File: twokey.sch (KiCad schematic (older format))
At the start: 10 parts, among them J1 12401610E4#2A, U1 ATSAMD21E18A-A, U2 MCP1700-3302E_SOT23

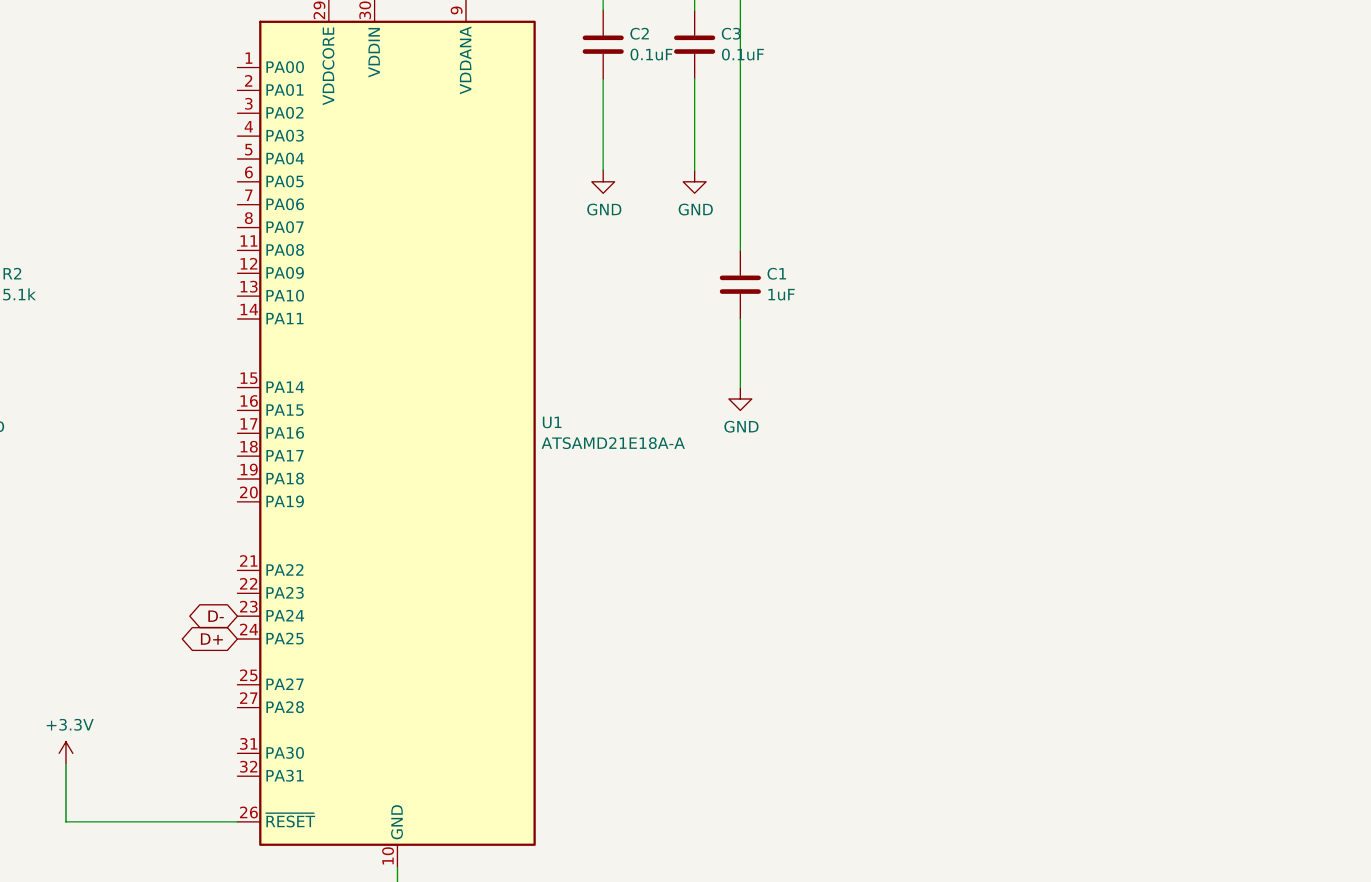
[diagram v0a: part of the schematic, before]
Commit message: added key switches
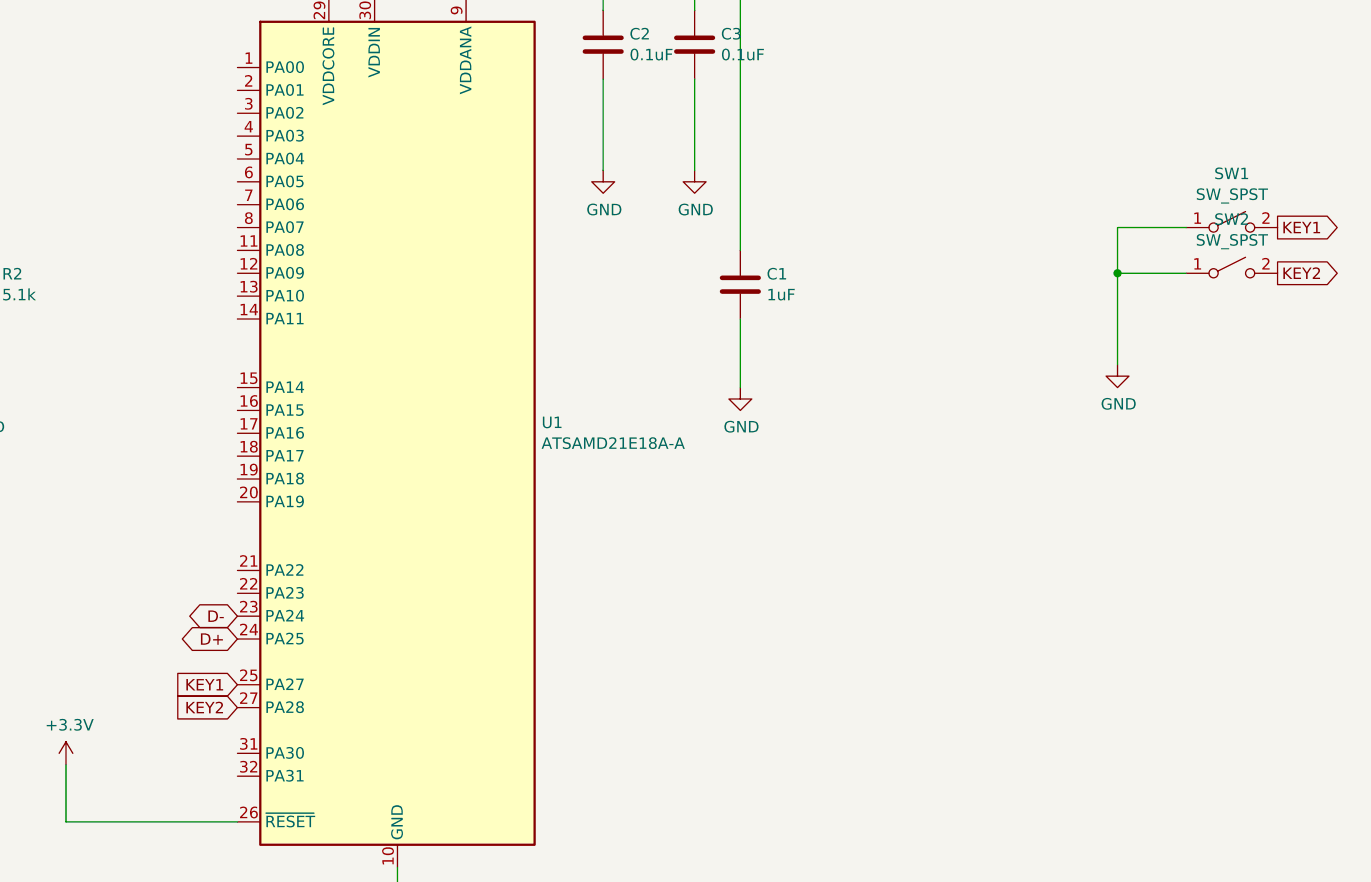
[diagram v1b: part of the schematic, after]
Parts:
- added SW1, SW2: SW_SPST, Button_Switch_Keyboard:SW_Cherry_MX_1.00u_PCB, symbol Switch:SW_SPST
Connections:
- net labels added: KEY1, KEY2
- wire segments 49 -> 53
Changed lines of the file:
@@
 Wire Wire Line
 	3450 3350 3450 3450
+$Comp
+L Switch:SW_SPST SW1
+U 1 1 60FA499B
+P 9150 2750
+F 0 "SW1" H 9150 2985 50  0000 C CNN
+F 1 "SW_SPST" H 9150 2894 50  0000 C CNN
+F 2 "Button_Switch_Keyboard:SW_Cherry_MX_1.00u_PCB" H 9150 2750 50  0001 C CNN
+F 3 "~" H 9150 2750 50  0001 C CNN
+	1    9150 2750
+	1    0    0    -1
+$EndComp
+Text GLabel 4800 4750 0    50   Input ~ 0
+KEY1
+Text GLabel 4800 4850 0    50   Input ~ 0
+KEY2
+Text GLabel 9350 2750 2    50   Output ~ 0
+KEY1
+$Comp
+L Switch:SW_SPST SW2
+U 1 1 60FA81CF
+P 9150 2950
+F 0 "SW2" H 9150 3185 50  0000 C CNN
+F 1 "SW_SPST" H 9150 3094 50  0000 C CNN
+F 2 "Button_Switch_Keyboard:SW_Cherry_MX_1.00u_PCB" H 9150 2950 50  0001 C CNN
+F 3 "~" H 9150 2950 50  0001 C CNN
+	1    9150 2950
+	1    0    0    -1
+$EndComp
+Text GLabel 9350 2950 2    50   Output ~ 0
+KEY2
+$Comp
+L power:GND #PWR016
+U 1 1 60FA8FBB
+P 8650 3350
+F 0 "#PWR016" H 8650 3100 50  0001 C CNN
+F 1 "GND" H 8655 3177 50  0000 C CNN
+F 2 "" H 8650 3350 50  0001 C CNN
+F 3 "" H 8650 3350 50  0001 C CNN
+	1    8650 3350
+	1    0    0    -1
+$EndComp
+Wire Wire Line
+	8950 2750 8650 2750
+Wire Wire Line
+	8650 2750 8650 2950
+Wire Wire Line
+	8950 2950 8650 2950
+Connection ~ 8650 2950
+Wire Wire Line
+	8650 2950 8650 3350
 $EndSCHEMATC

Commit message: ordered pcb
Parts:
- added D1, D2: BB-2020BGR-TRB, twokey:LED_BB-2020BGR-TRB, symbol BB-2020BGR-TRB:BB-2020BGR-TRB
- added J2: Conn_02x03_Odd_Even, twokey:TC2030-IDC-NL, symbol Connector_Generic:Conn_02x03_Odd_Even
- added U3: PTS526_SK15_SMTR2_LFS, twokey:PTS526 SK15 SMTR2 LFS, symbol 2021-07-27_21-35-03:PTS526_SK15_SMTR2_LFS
- U1: footprint Package_QFP:TQFP-32_7x7mm_P0.8mm -> Package_DFN_QFN:QFN-32-1EP_5x5mm_P0.5mm_EP3.6x3.6mm
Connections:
- net labels added: BUTTON, LED_CI, LED_DI, SWCLK, SWDIO, ~RESET
- wire segments 53 -> 63
- no-connect marks 0 -> 32
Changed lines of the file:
@@
 F 0 "U1" H 6130 3696 50  0000 L CNN
 F 1 "ATSAMD21E18A-A" H 6130 3605 50  0000 L CNN
-F 2 "Package_QFP:TQFP-32_7x7mm_P0.8mm" H 6400 1800 50  0001 C CNN
+F 2 "Package_DFN_QFN:QFN-32-1EP_5x5mm_P0.5mm_EP3.6x3.6mm" H 6400 1800 50  0001 C CNN
 F 3 "http://ww1.microchip.com/downloads/en/DeviceDoc/SAM_D21_DA1_Family_Data%20Sheet_DS40001882E.pdf" H 5500 3650 50  0001 C CNN
 	1    5500 3650
@@
 Wire Wire Line
 	7000 3150 7000 3450
-$Comp
-L power:+3.3V #PWR04
-U 1 1 60F4548C
-P 4050 5100
-F 0 "#PWR04" H 4050 4950 50  0001 C CNN
-F 1 "+3.3V" H 4065 5273 50  0000 C CNN
-F 2 "" H 4050 5100 50  0001 C CNN
-F 3 "" H 4050 5100 50  0001 C CNN
-	1    4050 5100
-	1    0    0    -1
-$EndComp
-Wire Wire Line
-	4050 5100 4050 5350
-Wire Wire Line
-	4050 5350 4800 5350
 $Comp
 L Device:C C2
@@
 	1    0    0    -1
 $EndComp
-Text GLabel 4800 4750 0    50   Input ~ 0
-KEY1
-Text GLabel 4800 4850 0    50   Input ~ 0
-KEY2
 Text GLabel 9350 2750 2    50   Output ~ 0
 KEY1
@@
 Wire Wire Line
 	8650 2950 8650 3350
+$Comp
+L BB-2020BGR-TRB:BB-2020BGR-TRB D1
+U 1 1 6100A1F5
+P 7900 5250
+F 0 "D1" H 7900 5817 50  0000 C CNN
+F 1 "BB-2020BGR-TRB" H 7900 5726 50  0000 C CNN
+F 2 "twokey:LED_BB-2020BGR-TRB" H 7900 5250 50  0001 L BNN
+F 3 "" H 7900 5250 50  0001 L BNN
+F 4 "--" H 7900 5250 50  0001 L BNN "PARTREV"
+F 5 "American Bright LED" H 7900 5250 50  0001 L BNN "MANUFACTURER"
+F 6 "0.75mm" H 7900 5250 50  0001 L BNN "MAXIMUM_PACKAGE_HEIGHT"
+F 7 "Manufacturer recommendations" H 7900 5250 50  0001 L BNN "STANDARD"
+	1    7900 5250
+	1    0    0    -1
+$EndComp
+$Comp
+L Connector_Generic:Conn_02x03_Odd_Even J2
+U 1 1 610124D7
+P 9300 1600
+F 0 "J2" H 9350 1917 50  0000 C CNN
+F 1 "Conn_02x03_Odd_Even" H 9350 1826 50  0000 C CNN
+F 2 "twokey:TC2030-IDC-NL" H 9300 1600 50  0001 C CNN
+F 3 "~" H 9300 1600 50  0001 C CNN
+	1    9300 1600
+	1    0    0    -1
+$EndComp
+$Comp
+L power:GND #PWR019
+U 1 1 61013843
+P 8850 1950
+F 0 "#PWR019" H 8850 1700 50  0001 C CNN
+F 1 "GND" H 8855 1777 50  0000 C CNN
+F 2 "" H 8850 1950 50  0001 C CNN
+F 3 "" H 8850 1950 50  0001 C CNN
+	1    8850 1950
+	1    0    0    -1
+$EndComp
+Wire Wire Line
+	9100 1700 8850 1700
+Wire Wire Line
+	8850 1700 8850 1950
+$Comp
+L power:+3.3V #PWR018
+U 1 1 610159A3
+P 8850 1150
+F 0 "#PWR018" H 8850 1000 50  0001 C CNN
+F 1 "+3.3V" H 8865 1323 50  0000 C CNN
+F 2 "" H 8850 1150 50  0001 C CNN
+F 3 "" H 8850 1150 50  0001 C CNN
+	1    8850 1150
+	1    0    0    -1
+$EndComp
+Wire Wire Line
+	8850 1150 8850 1500
+Wire Wire Line
+	8850 1500 9100 1500
+Text GLabel 9100 1600 0    50   Output ~ 0
+~RESET
+Text GLabel 4800 5350 0    50   Input ~ 0
+~RESET
+Text GLabel 4800 5150 0    50   BiDi ~ 0
+SWDIO
+Text GLabel 9600 1500 2    50   BiDi ~ 0
+SWDIO
+Text GLabel 9600 1600 2    50   Output ~ 0
+SWCLK
+Text GLabel 4800 5050 0    50   Input ~ 0
+SWCLK
+NoConn ~ 9600 1700
+NoConn ~ 4800 2150
+NoConn ~ 4800 2250
+NoConn ~ 4800 2350
+NoConn ~ 4800 2450
+NoConn ~ 4800 2550
+NoConn ~ 4800 2950
+NoConn ~ 4800 3050
+NoConn ~ 4800 3150
+NoConn ~ 4800 3650
+NoConn ~ 4800 3750
+NoConn ~ 4800 3850
+NoConn ~ 4800 3950
+NoConn ~ 4800 4250
+NoConn ~ 4800 4350
+NoConn ~ 1950 3000
+NoConn ~ 1950 2700
+NoConn ~ 1950 2900
+NoConn ~ 1950 2200
+NoConn ~ 1950 2100
+NoConn ~ 3150 2100
+NoConn ~ 3150 2200
+NoConn ~ 3150 2400
+NoConn ~ 3150 2900
+NoConn ~ 3150 3000
+$Comp
+L power:GND #PWR017
+U 1 1 6103CE75
+P 8700 5850
+F 0 "#PWR017" H 8700 5600 50  0001 C CNN
+F 1 "GND" H 8705 5677 50  0000 C CNN
+F 2 "" H 8700 5850 50  0001 C CNN
+F 3 "" H 8700 5850 50  0001 C CNN
+	1    8700 5850
+	1    0    0    -1
+$EndComp
+$Comp
+L power:GND #PWR020
+U 1 1 6103D8BF
+P 10600 5800
+F 0 "#PWR020" H 10600 5550 50  0001 C CNN
+F 1 "GND" H 10605 5627 50  0000 C CNN
+F 2 "" H 10600 5800 50  0001 C CNN
+F 3 "" H 10600 5800 50  0001 C CNN
+	1    10600 5800
+	1    0    0    -1
+$EndComp
+Wire Wire Line
+	8500 5450 8700 5450
+Wire Wire Line
+	8700 5450 8700 5850
+Wire Wire Line
+	10300 5450 10600 5450
+Wire Wire Line
+	10600 5450 10600 5800
+Text GLabel 8500 4950 2    50   Input ~ 0
+VBUS
+Text GLabel 10300 4950 2    50   Input ~ 0
+VBUS
+Wire Wire Line
+	8500 5150 9100 5150
+Wire Wire Line
+	8500 5250 9100 5250
+$Comp
+L BB-2020BGR-TRB:BB-2020BGR-TRB D2
+U 1 1 6100ACA2
+P 9700 5250
+F 0 "D2" H 9700 5817 50  0000 C CNN
+F 1 "BB-2020BGR-TRB" H 9700 5726 50  0000 C CNN
+F 2 "twokey:LED_BB-2020BGR-TRB" H 9700 5250 50  0001 L BNN
+F 3 "" H 9700 5250 50  0001 L BNN
+F 4 "--" H 9700 5250 50  0001 L BNN "PARTREV"
+F 5 "American Bright LED" H 9700 5250 50  0001 L BNN "MANUFACTURER"
+F 6 "0.75mm" H 9700 5250 50  0001 L BNN "MAXIMUM_PACKAGE_HEIGHT"
+F 7 "Manufacturer recommendations" H 9700 5250 50  0001 L BNN "STANDARD"
+	1    9700 5250
+	1    0    0    -1
+$EndComp
+NoConn ~ 10300 5150
+NoConn ~ 10300 5250
+Text GLabel 7300 5150 0    50   Input ~ 0
+LED_DI
+Text GLabel 7300 5250 0    50   Input ~ 0
+LED_CI
+$Comp
+L 2021-07-27_21-35-03:PTS526_SK15_SMTR2_LFS U3
+U 1 1 6104711C
+P 3050 6800
+F 0 "U3" H 3850 7187 60  0000 C CNN
+F 1 "PTS526_SK15_SMTR2_LFS" H 3850 7081 60  0000 C CNN
+F 2 "twokey:PTS526 SK15 SMTR2 LFS" H 3850 7040 60  0001 C CNN
+F 3 "" H 3050 6800 60  0000 C CNN
+	1    3050 6800
+	1    0    0    -1
+$EndComp
+NoConn ~ 3050 6900
+NoConn ~ 4650 6900
+Text GLabel 3050 6800 0    50   Output ~ 0
+BUTTON
+$Comp
+L power:GND #PWR04
+U 1 1 61049E96
+P 5000 7150
+F 0 "#PWR04" H 5000 6900 50  0001 C CNN
+F 1 "GND" H 5005 6977 50  0000 C CNN
+F 2 "" H 5000 7150 50  0001 C CNN
+F 3 "" H 5000 7150 50  0001 C CNN
+	1    5000 7150
+	1    0    0    -1
+$EndComp
+Wire Wire Line
+	4650 6800 5000 6800
+Wire Wire Line
+	5000 6800 5000 7150
+Text GLabel 4800 3550 0    50   Input ~ 0
+KEY1
+Text GLabel 4800 3450 0    50   Input ~ 0
+KEY2
+NoConn ~ 4800 4750
+NoConn ~ 4800 4850
+Text GLabel 4800 2650 0    50   Input ~ 0
+LED_DI
+Text GLabel 4800 2750 0    50   Input ~ 0
+LED_CI
+NoConn ~ 4800 2850
+Text GLabel 4800 2050 0    50   Input ~ 0
+BUTTON
 $EndSCHEMATC

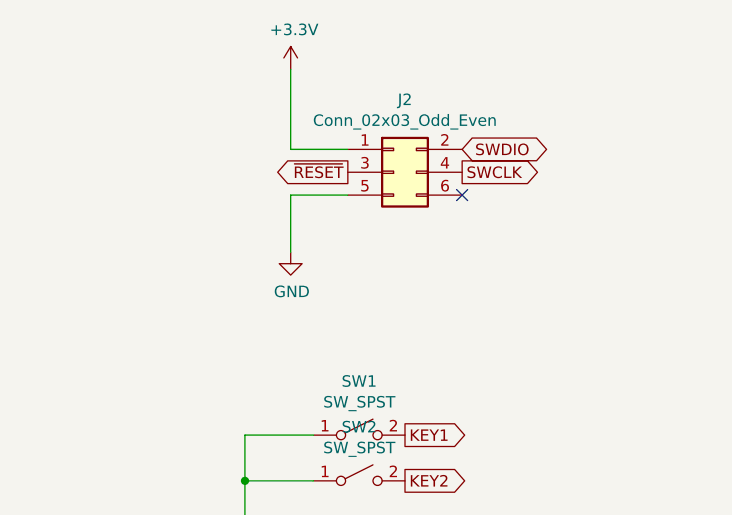
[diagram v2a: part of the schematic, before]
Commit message: switched components to top. ordered new board
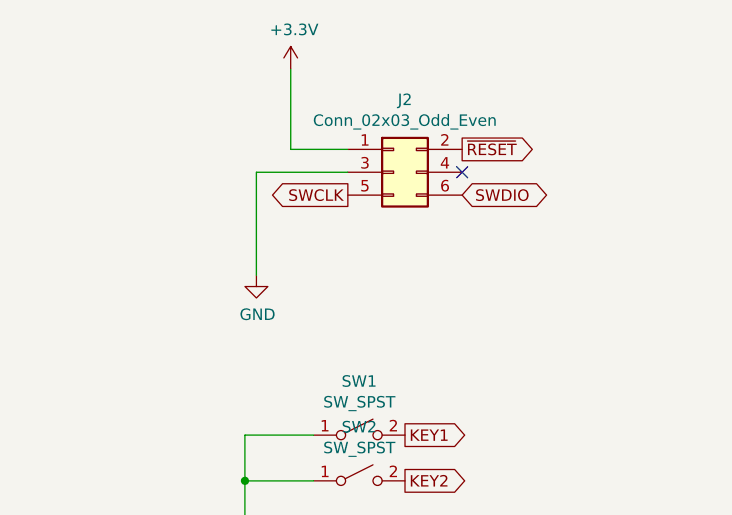
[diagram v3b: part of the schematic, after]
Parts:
- J1: footprint 12401610E4_2A:AMPHENOL_12401610E4#2A -> twokey:USB_C_Receptacle_GT-USB-7010
- SW1, SW2: footprint Button_Switch_Keyboard:SW_Cherry_MX_1.00u_PCB -> twokey:Kailh_socket_MX
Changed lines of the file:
@@
 F 0 "J1" H 2550 3467 50  0000 C CNN
 F 1 "12401610E4#2A" H 2550 3376 50  0000 C CNN
-F 2 "12401610E4_2A:AMPHENOL_12401610E4#2A" H 2550 2600 50  0001 L BNN
+F 2 "twokey:USB_C_Receptacle_GT-USB-7010" H 2550 2600 50  0001 L BNN
 F 3 "Manufacturer Recommendation" H 2550 2600 50  0001 L BNN
 F 4 "12401610E4#2A" H 2550 2600 50  0001 L BNN "Field4"
@@
 F 0 "SW1" H 9150 2985 50  0000 C CNN
 F 1 "SW_SPST" H 9150 2894 50  0000 C CNN
-F 2 "Button_Switch_Keyboard:SW_Cherry_MX_1.00u_PCB" H 9150 2750 50  0001 C CNN
+F 2 "twokey:Kailh_socket_MX" H 9150 2750 50  0001 C CNN
 F 3 "~" H 9150 2750 50  0001 C CNN
 	1    9150 2750
@@
 F 0 "SW2" H 9150 3185 50  0000 C CNN
 F 1 "SW_SPST" H 9150 3094 50  0000 C CNN
-F 2 "Button_Switch_Keyboard:SW_Cherry_MX_1.00u_PCB" H 9150 2950 50  0001 C CNN
+F 2 "twokey:Kailh_socket_MX" H 9150 2950 50  0001 C CNN
 F 3 "~" H 9150 2950 50  0001 C CNN
 	1    9150 2950
@@
 $EndComp
 $Comp
-L power:GND #PWR019
-U 1 1 61013843
-P 8850 1950
-F 0 "#PWR019" H 8850 1700 50  0001 C CNN
-F 1 "GND" H 8855 1777 50  0000 C CNN
-F 2 "" H 8850 1950 50  0001 C CNN
-F 3 "" H 8850 1950 50  0001 C CNN
-	1    8850 1950
-	1    0    0    -1
-$EndComp
-Wire Wire Line
-	9100 1700 8850 1700
-Wire Wire Line
-	8850 1700 8850 1950
-$Comp
 L power:+3.3V #PWR018
 U 1 1 610159A3
@@
 Wire Wire Line
 	8850 1500 9100 1500
-Text GLabel 9100 1600 0    50   Output ~ 0
+Text GLabel 9600 1500 2    50   Output ~ 0
 ~RESET
 Text GLabel 4800 5350 0    50   Input ~ 0
@@
 Text GLabel 4800 5150 0    50   BiDi ~ 0
 SWDIO
-Text GLabel 9600 1500 2    50   BiDi ~ 0
+Text GLabel 9600 1700 2    50   BiDi ~ 0
 SWDIO
-Text GLabel 9600 1600 2    50   Output ~ 0
+Text GLabel 9100 1700 0    50   Output ~ 0
 SWCLK
 Text GLabel 4800 5050 0    50   Input ~ 0
 SWCLK
-NoConn ~ 9600 1700
 NoConn ~ 4800 2150
 NoConn ~ 4800 2250
@@
 Text GLabel 4800 2050 0    50   Input ~ 0
 BUTTON
+Wire Wire Line
+	9100 1600 8700 1600
+Wire Wire Line
+	8700 1600 8700 2050
+$Comp
+L power:GND #PWR0101
+U 1 1 61145E72
+P 8700 2050
+F 0 "#PWR0101" H 8700 1800 50  0001 C CNN
+F 1 "GND" H 8705 1877 50  0000 C CNN
+F 2 "" H 8700 2050 50  0001 C CNN
+F 3 "" H 8700 2050 50  0001 C CNN
+	1    8700 2050
+	1    0    0    -1
+$EndComp
+NoConn ~ 9600 1600
 $EndSCHEMATC
